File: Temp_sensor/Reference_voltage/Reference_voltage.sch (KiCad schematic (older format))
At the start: 57 parts, among them J1 CN3, J2 CN4, SW1 SW_DIP_x01, SW2 SW_DIP_x01, U1 HDSP-7401_Paulo, U2 HDSP-7401_Paulo, U3 HDSP-7401_Paulo, U4 HDSP-7401_Paulo, U5 LM4128, U6 74HC595, U7 74HC595, U8 74HC595, U9 74HC595

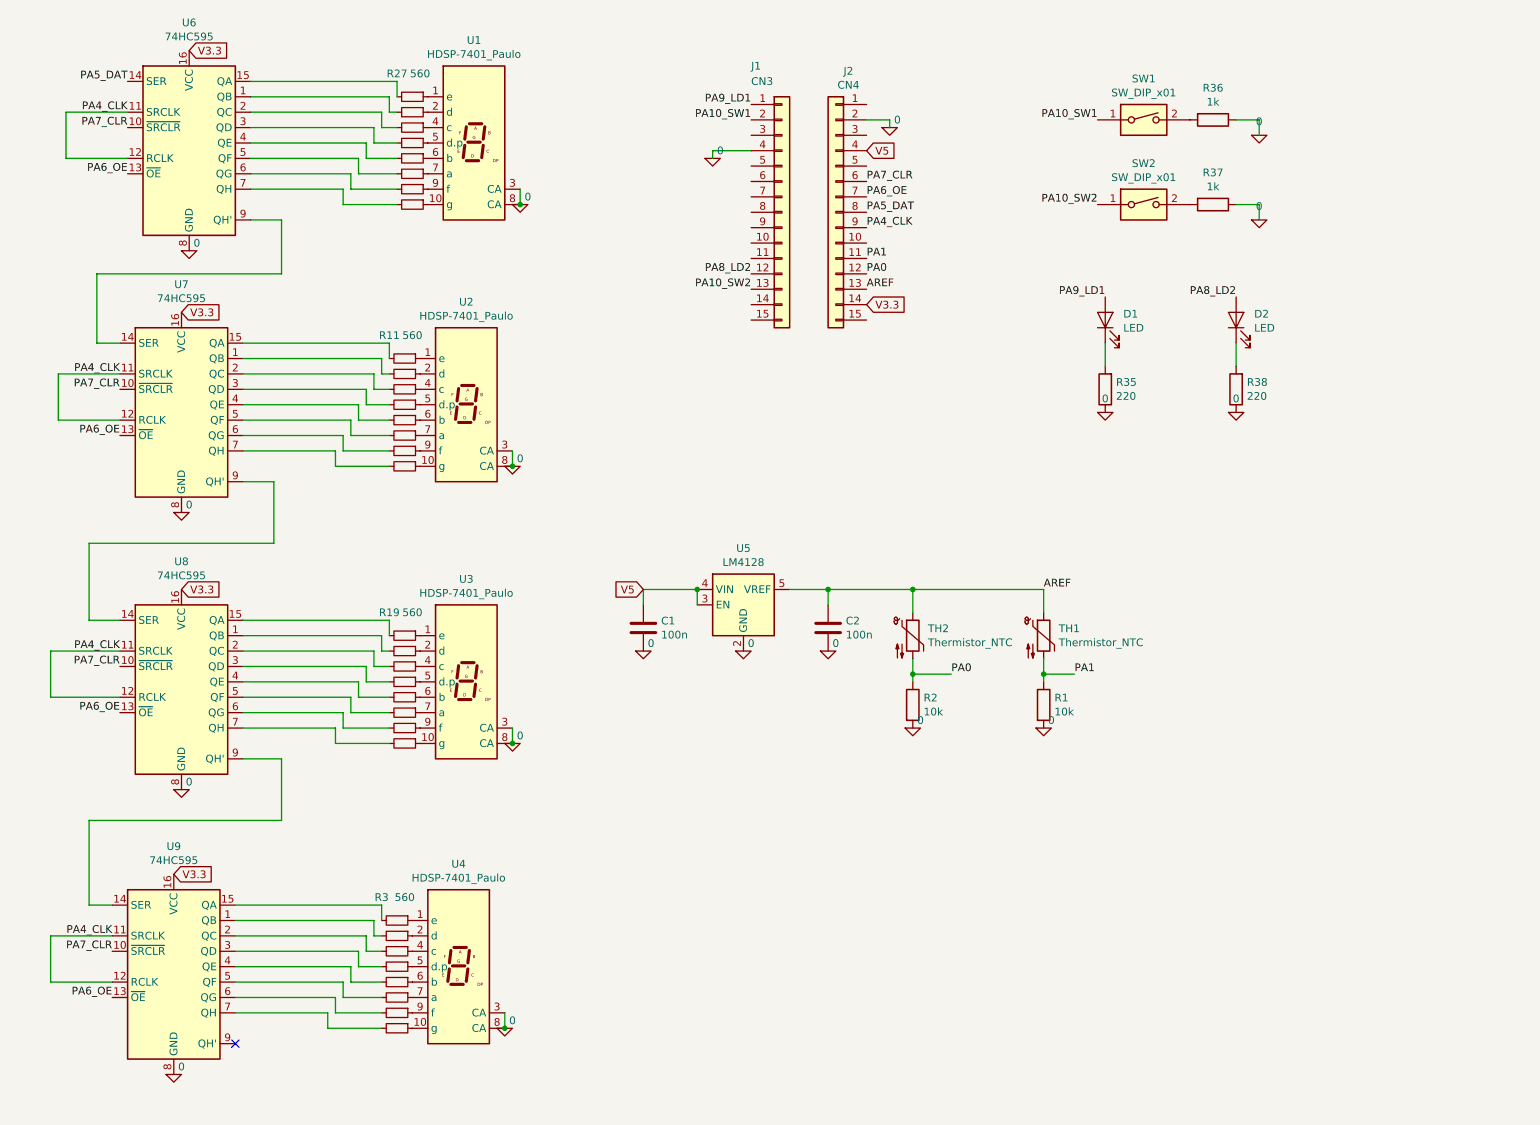
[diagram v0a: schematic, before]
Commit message: Through Hole to SMD components
first print of the board
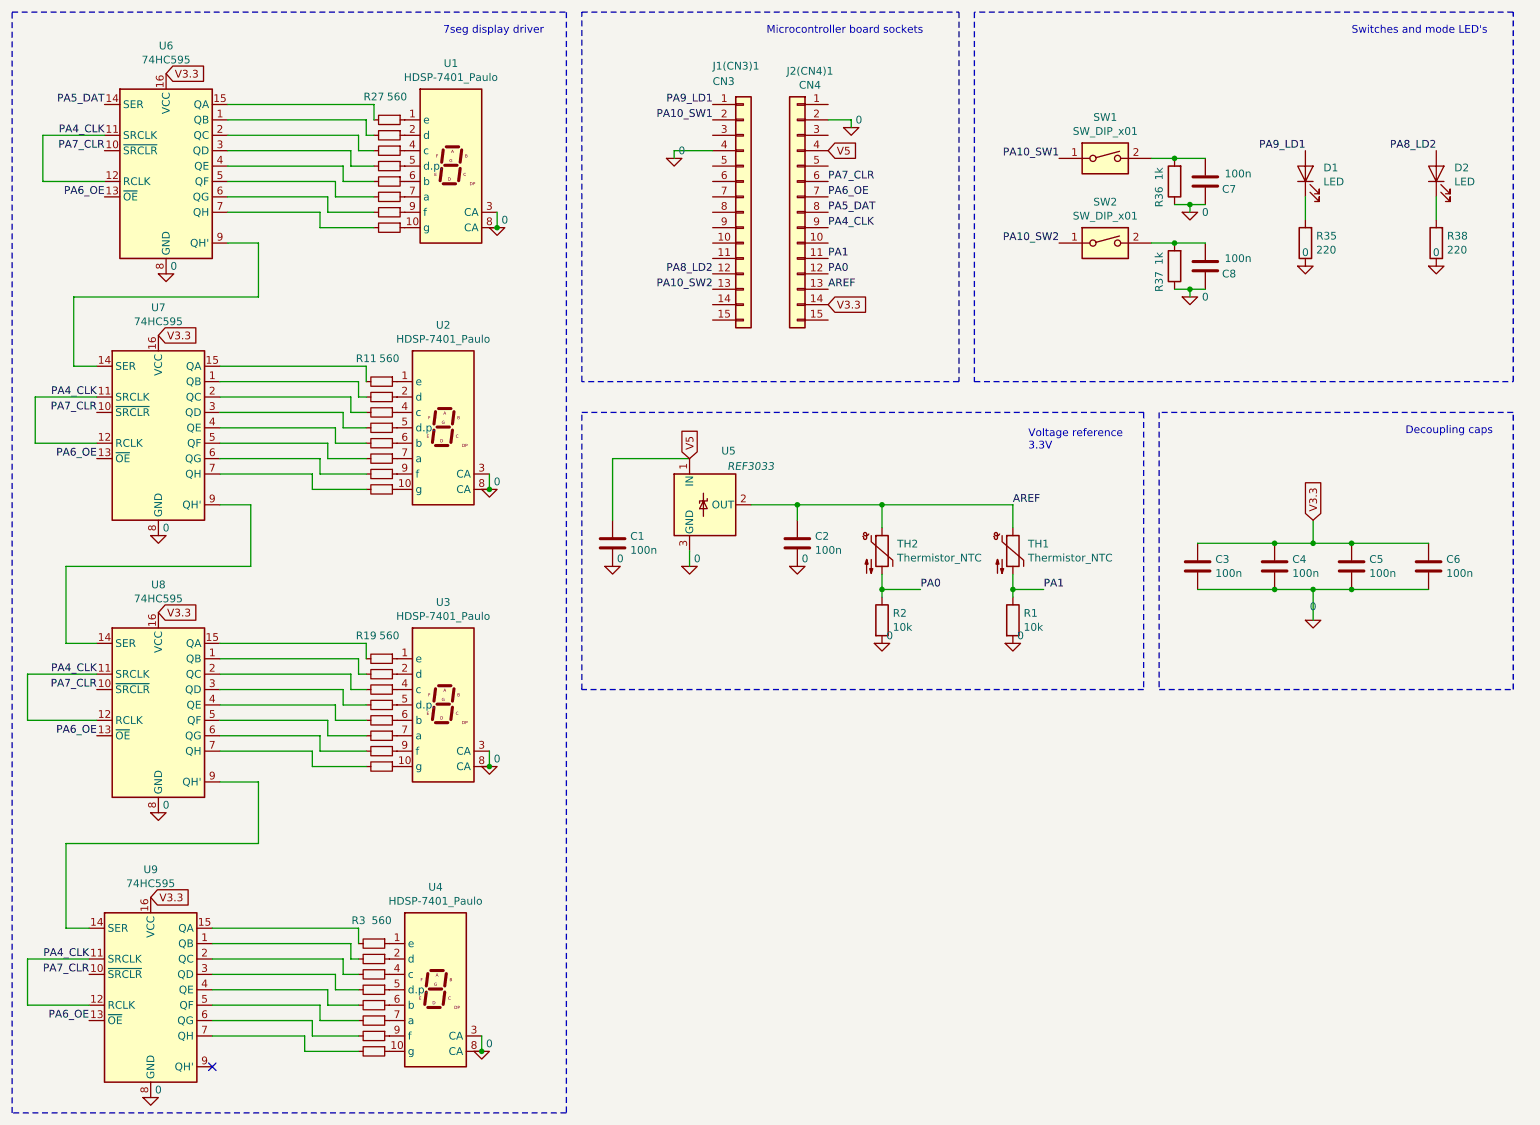
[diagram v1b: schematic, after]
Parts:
- removed U5: LM4128, Package_TO_SOT_SMD:SOT-23-5, symbol Reference_Voltage:LM4128
- added C3, C4, C5, C6, C7, C8: 100n, Capacitor_SMD:C_0805_2012Metric_Pad1.15x1.40mm_HandSolder, symbol Device:C
- added U5: REF3033, Package_TO_SOT_SMD:SOT-23_Handsoldering, symbol Reference_Voltage:REF3033
- C1, C2: footprint Capacitor_THT:C_Rect_L7.2mm_W2.5mm_P5.00mm_FKS2_FKP2_MKS2_MKP2 -> Capacitor_SMD:C_0805_2012Metric_Pad1.15x1.40mm_HandSolder
- D1, D2: footprint LED_THT:LED_D4.0mm -> LED_SMD:LED_0805_2012Metric_Pad1.15x1.40mm_HandSolder
- R1, R10, R11, R12, R13, R14, R15, R16, R17, R18, R19, R2, R20, R21, R22, R23, R24, R25, R26, R27, R28, R29, R3, R30, R31, R32, R33, R34, R35, R36, R37, R38, R4, R5, R6, R7, R8, R9: footprint Resistor_THT:R_Axial_DIN0309_L9.0mm_D3.2mm_P12.70mm_Horizontal -> Resistor_SMD:R_0805_2012Metric_Pad1.15x1.40mm_HandSolder
- U6, U7, U8, U9: footprint Package_DIP:DIP-16_W7.62mm_LongPads -> Package_SO:SOIC-16_3.9x9.9mm_P1.27mm
- renumbered J1 to J1(CN3)1, J2 to J2(CN4)1
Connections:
- net 0: now also C3.2, C4.2, C5.2, C6.2, C7.1, C8.1, U5.3 (GND)
- net AREF~: now also U5.2 (OUT)
- net V3.3: now also C3.1, C4.1, C5.1, C6.1
- net V5: now also U5.1 (IN)
- net at R36.2, SW1.2: now also C7.2
- net at R37.2, SW2.2: now also C8.2
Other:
- note added: "7seg display driver\n"
- note added: "Decoupling caps"
- note added: "Microcontroller board sockets"
- note added: "Switches and mode LED's\n"
- note added: "Voltage reference\n3.3V"
- moved on the sheet: C1, C2, D1, D2, J1(CN3)1, J2(CN4)1, R1, R11, R19, R2, R27, R3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
